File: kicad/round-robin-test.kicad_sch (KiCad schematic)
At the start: 22 parts, among them SW1 SW_Push, SW1 SW_SPDT, SW2 SW_Push, SW3 SW_Push, SW4 SW_Push, SW5 SW_Push, SW6 SW_Push

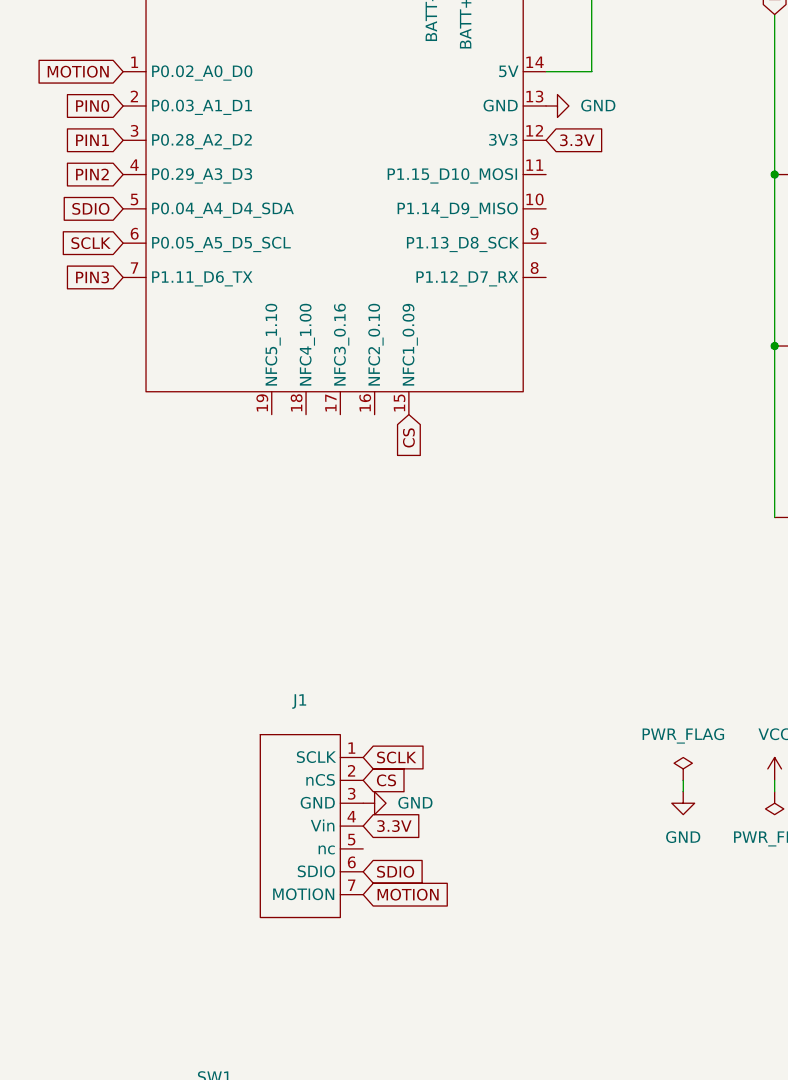
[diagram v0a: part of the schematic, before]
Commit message: fixed pin numbers
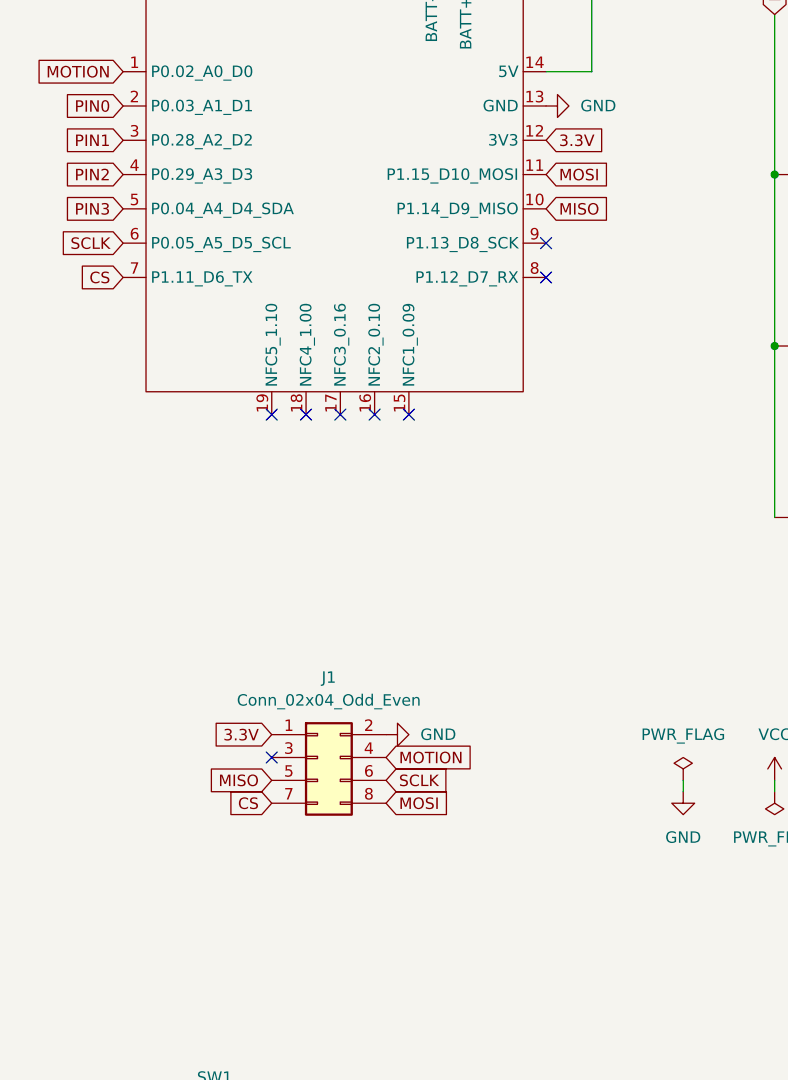
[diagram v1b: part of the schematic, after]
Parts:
- removed J1: ~, myfootprintLibrary:pmw3610_connector, symbol roBa-Keyboard:pmw3610_breakout
- added J1: Conn_02x04_Odd_Even, Connector_PinHeader_2.54mm:PinHeader_2x04_P2.54mm_Vertical, symbol Connector_Generic:Conn_02x04_Odd_Even
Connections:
- net SDIO is gone; now on net PIN3: U1.5 (P0.04_A4_D4_SDA)
- net 3.3V: now also J1.1 (Pin_1)
- net CS: now also U1.7 (P1.11_D6_TX), J1.7 (Pin_7); no longer U1.15 (NFC1_0.09)
- net GND: now also J1.2 (Pin_2)
- net MOTION: now also J1.4 (Pin_4)
- net PIN3: no longer U1.7 (P1.11_D6_TX)
- net SCLK: now also J1.6 (Pin_6)
- net MISO: now reaches U1.10 (P1.14_D9_MISO)
- net MISO: now also J1.5 (Pin_5)
- net MOSI: now reaches U1.11 (P1.15_D10_MOSI)
- net MOSI: now also J1.8 (Pin_8)
- no-connect marks 0 -> 8

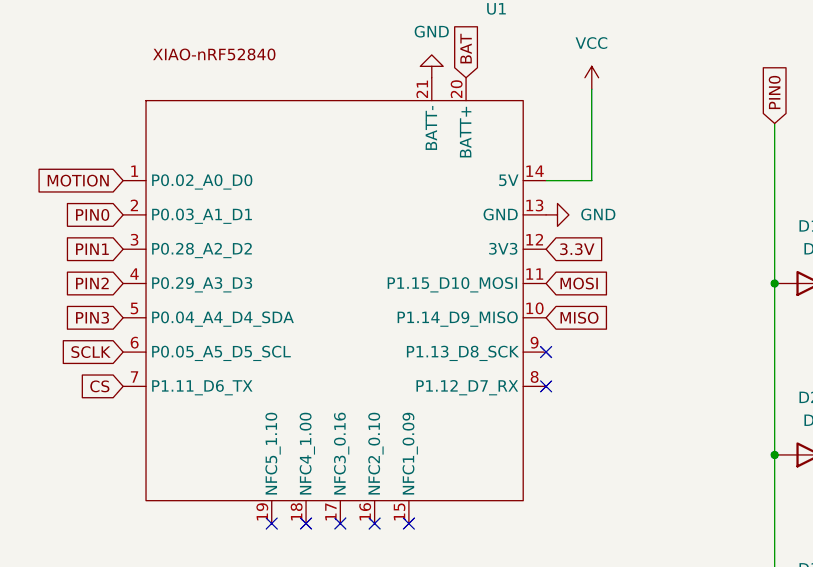
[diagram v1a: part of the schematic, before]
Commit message: fixed spi pin numbers
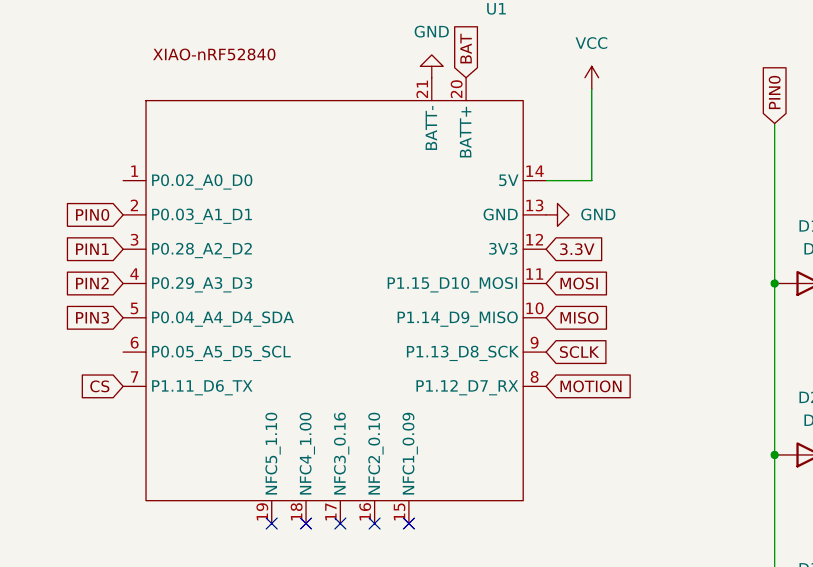
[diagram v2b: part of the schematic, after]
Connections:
- net MOTION: now also U1.8 (P1.12_D7_RX); no longer U1.1 (P0.02_A0_D0)
- net SCLK: now also U1.9 (P1.13_D8_SCK); no longer U1.6 (P0.05_A5_D5_SCL)
- no-connect marks 8 -> 6
